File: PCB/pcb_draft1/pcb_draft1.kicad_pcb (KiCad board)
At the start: 2 copper layers, 100 x 100 mm, 53 parts, among them Q1 DMN6140L, Q10 DMN6140L, Q11 DMN6140L, Q12 DMN6140L, Q13 DMN6140L, Q14 DMN6140L, Q2 DMN6140L, Q3 DMN6140L, Q4 DMN6140L, Q5 DMN6140L, Q6 DMN6140L, Q7 DMN6140L, Q8 DMN6140L, Q9 DMN6140L, U1 STSPIN820, U2 STSPIN820

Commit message: add new netlist
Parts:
- added Arduino_FanControl1: Conn_01x01_Male, Connector_PinHeader_2.54mm:PinHeader_1x01_P2.54mm_Vertical, F.Cu at (177.5, -15.1)
- added D15: 1N4003, Diode_THT:D_DO-41_SOD81_P10.16mm_Horizontal, F.Cu at (165.0, -23.6)
- added Fan_Out1: Screw_Terminal_01x02, TerminalBlock_Phoenix:TerminalBlock_Phoenix_MKDS-1,5-2_1x02_P5.00mm_Horizontal, F.Cu at (166.6, -15.2)
- added Q15: DMN6140L, custom_symbols:SOT-223-edited, F.Cu at (182.0, -21.6)
- added R15: 200_Ohm_R, Resistor_SMD:R_0603_1608Metric, F.Cu at (189.4, -24.5)
- R1, R10, R11, R12, R13, R14, R2, R3, R4, R5, R6, R7, R8, R9: value R_Small -> 200_Ohm_R
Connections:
- U1 pad 2: GND -> 5V
- U1 pad 3: GND -> 5V
- U2 pad 2: GND -> 5V
- U2 pad 3: GND -> 5V

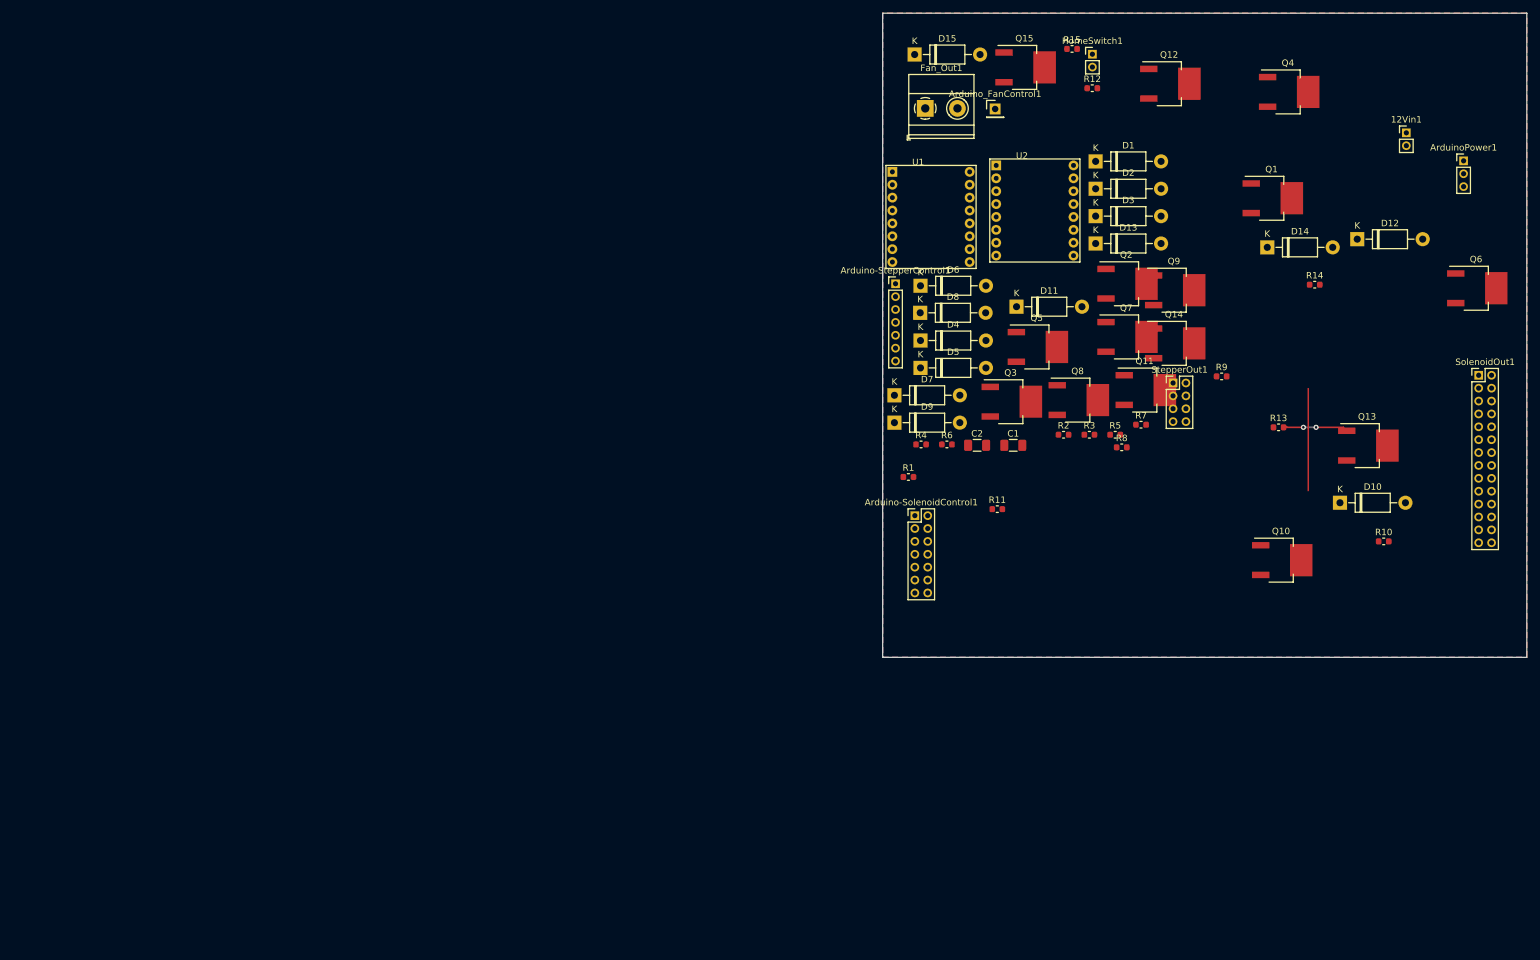
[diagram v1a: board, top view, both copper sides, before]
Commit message: Run traces for preliminarily finished board
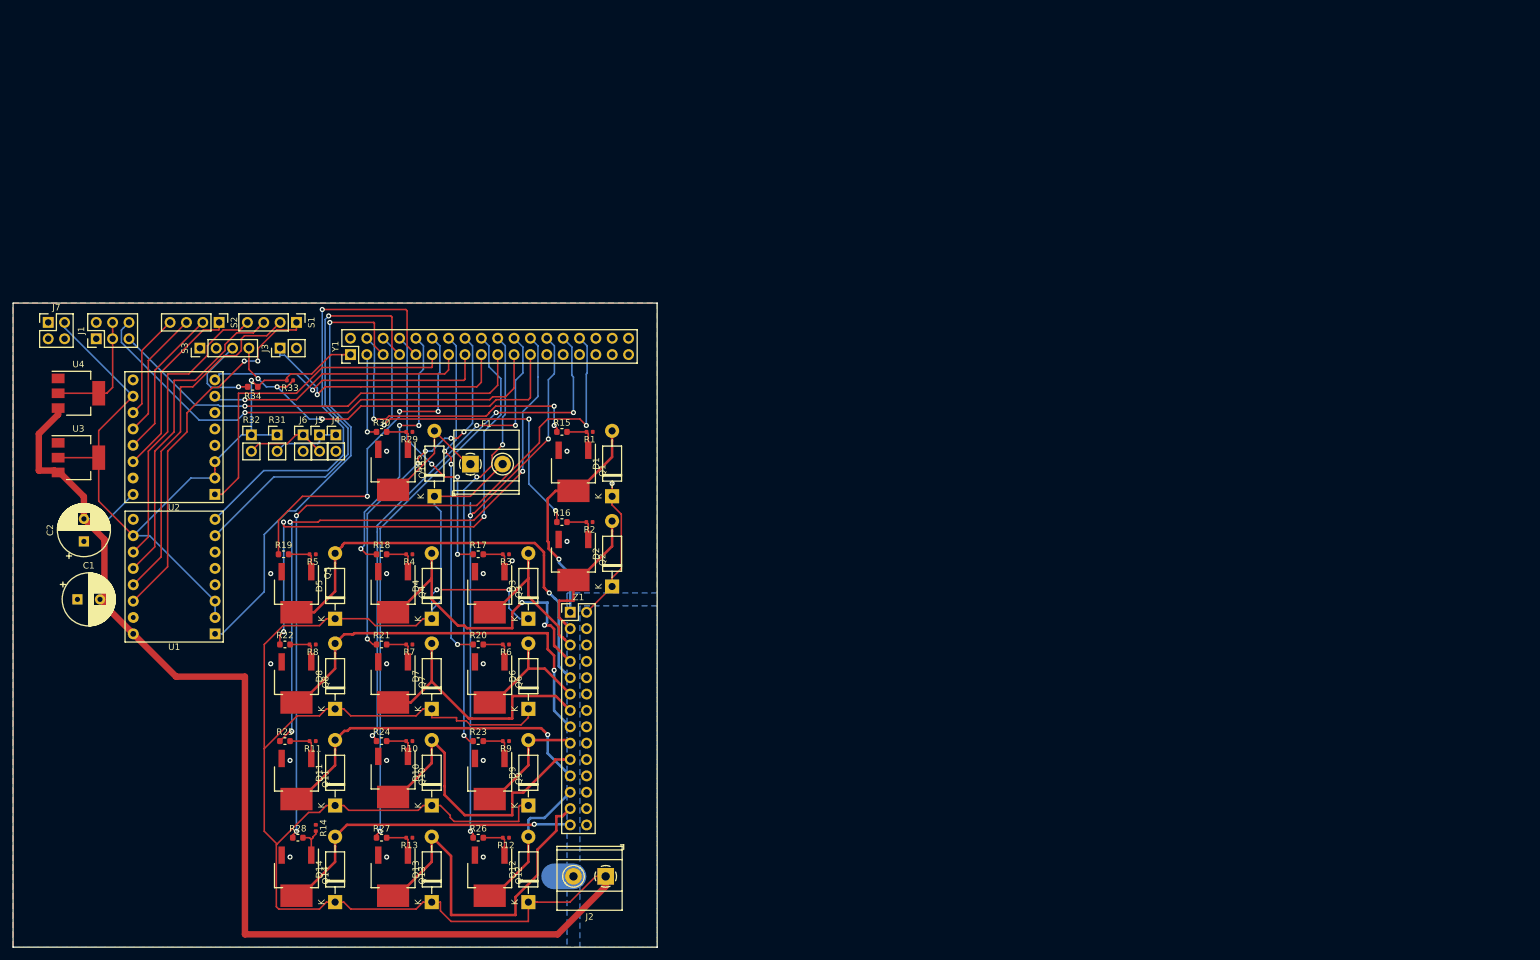
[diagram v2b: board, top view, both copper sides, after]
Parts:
- removed 12Vin1, HomeSwitch1: Conn_01x02_Male, Connector_PinHeader_2.00mm:PinHeader_1x02_P2.00mm_Vertical
- removed Arduino-SolenoidControl1: Conn_02x07_Odd_Even, Connector_PinHeader_2.00mm:PinHeader_2x07_P2.00mm_Vertical
- removed Arduino-StepperControl1: Conn_01x07_Male, Connector_PinHeader_2.00mm:PinHeader_1x07_P2.00mm_Vertical
- removed ArduinoPower1: Conn_01x03_Male, Connector_PinHeader_2.00mm:PinHeader_1x03_P2.00mm_Vertical
- removed Arduino_FanControl1: Conn_01x01_Male, Connector_PinHeader_2.54mm:PinHeader_1x01_P2.54mm_Vertical
- removed Fan_Out1: Screw_Terminal_01x02, TerminalBlock_Phoenix:TerminalBlock_Phoenix_MKDS-1,5-2_1x02_P5.00mm_Horizontal
- removed SolenoidOut1: Conn_02x14_Odd_Even, Connector_PinHeader_2.00mm:PinHeader_2x14_P2.00mm_Vertical
- removed StepperOut1: Conn_02x04_Odd_Even, Connector_PinHeader_2.00mm:PinHeader_2x04_P2.00mm_Vertical
- added F1: Fan_Screw_Terminal A97996-ND, TerminalBlock_Phoenix:TerminalBlock_Phoenix_MKDS-1,5-2_1x02_P5.00mm_Horizontal, F.Cu at (96.0, 40.0)
- added J1: RollerServos, Connector_PinHeader_2.54mm:PinHeader_2x03_P2.54mm_Vertical, F.Cu at (37.9, 20.5)
- added J2: 12V_Power A97996-ND, TerminalBlock_Phoenix:TerminalBlock_Phoenix_MKDS-1,5-2_1x02_P5.00mm_Horizontal, F.Cu at (117.0, 104.0)
- added J3: HomeSwitch, Connector_PinHeader_2.54mm:PinHeader_1x02_P2.54mm_Vertical, F.Cu at (66.5, 22.0)
- added J4: Therm1, Connector_PinHeader_2.54mm:PinHeader_1x02_P2.54mm_Vertical, F.Cu at (75.1, 35.5)
- added J5: ArdAnalogTherm, Connector_PinHeader_2.54mm:PinHeader_1x02_P2.54mm_Vertical, F.Cu at (72.6, 35.5)
- added J6: Therm2, Connector_PinHeader_2.54mm:PinHeader_1x02_P2.54mm_Vertical, F.Cu at (70.0, 35.5)
- added J7: Conn_02x02_Odd_Even, Connector_PinHeader_2.54mm:PinHeader_2x02_P2.54mm_Vertical, F.Cu at (30.5, 18.0)
- added R16: 200_Ohm_R, Resistor_SMD:R_0603_1608Metric, F.Cu at (110.2, 49.0)
- added R17: 200_Ohm_R, Resistor_SMD:R_0603_1608Metric, F.Cu at (97.2, 54.0)
- added R18: 200_Ohm_R, Resistor_SMD:R_0603_1608Metric, F.Cu at (82.2, 54.0)
- added R19: 200_Ohm_R, Resistor_SMD:R_0603_1608Metric, F.Cu at (67.0, 54.0)
- added R20: 200_Ohm_R, Resistor_SMD:R_0603_1608Metric, F.Cu at (97.2, 68.0)
- added R21: 200_Ohm_R, Resistor_SMD:R_0603_1608Metric, F.Cu at (82.2, 68.0)
- added R22: 200_Ohm_R, Resistor_SMD:R_0603_1608Metric, F.Cu at (67.2, 68.0)
- added R23: 200_Ohm_R, Resistor_SMD:R_0603_1608Metric, F.Cu at (97.2, 83.0)
- added R24: 200_Ohm_R, Resistor_SMD:R_0603_1608Metric, F.Cu at (82.2, 83.0)
- added R25: 200_Ohm_R, Resistor_SMD:R_0603_1608Metric, F.Cu at (67.2, 83.0)
- added R26: 200_Ohm_R, Resistor_SMD:R_0603_1608Metric, F.Cu at (97.2, 98.0)
- added R27: 200_Ohm_R, Resistor_SMD:R_0603_1608Metric, F.Cu at (82.2, 98.0)
- added R28: 200_Ohm_R, Resistor_SMD:R_0603_1608Metric, F.Cu at (69.2, 98.0)
- added R29: 10K_Ohm_R, Resistor_SMD:R_0402_1005Metric, F.Cu at (86.5, 35.0)
- added R30: 200_Ohm_R, Resistor_SMD:R_0603_1608Metric, F.Cu at (82.2, 35.0)
- added R31: ThermistorR, Connector_PinHeader_2.54mm:PinHeader_1x02_P2.54mm_Vertical, F.Cu at (66.0, 35.5)
- added R32: ThermistorR, Connector_PinHeader_2.54mm:PinHeader_1x02_P2.54mm_Vertical, F.Cu at (62.0, 35.5)
- added R33: 2.7k_Ohm_Res, Resistor_SMD:R_0402_1005Metric, F.Cu at (68.0, 27.0)
- added R34: 250_Ohm_Resistor, Resistor_SMD:R_0603_1608Metric, F.Cu at (62.2, 28.0)
- added S1: StepperMotor1, Connector_PinHeader_2.54mm:PinHeader_1x04_P2.54mm_Vertical, F.Cu at (69.0, 18.0)
- added S2: StepperMotor2, Connector_PinHeader_2.54mm:PinHeader_1x04_P2.54mm_Vertical, F.Cu at (57.0, 18.0)
- added S3: PaperHome, Connector_PinHeader_2.54mm:PinHeader_1x04_P2.54mm_Vertical, F.Cu at (54.0, 22.0)
- added U3: AMS1117-5.0 RasPi, Package_TO_SOT_SMD:SOT-223-3_TabPin2, F.Cu at (35.1, 39.0)
- added U4: AMS1117-5.0 Servo, Package_TO_SOT_SMD:SOT-223-3_TabPin2, F.Cu at (35.1, 29.0)
- added Y1: Arduino_Mega_Bottom_Pins1, Connector_PinHeader_2.54mm:PinHeader_2x18_P2.54mm_Vertical, F.Cu at (77.4, 23.0)
- added Z1: SolenoidOut, Connector_PinHeader_2.54mm:PinHeader_2x14_P2.54mm_Vertical, F.Cu at (111.5, 63.0)
- C1, C2: footprint Capacitor_SMD:C_1206_3216Metric -> Capacitor_THT:CP_Radial_D8.0mm_P3.50mm
- R1, R10, R11, R12, R13, R14, R2, R3, R4, R5, R6, R7, R8, R9: value 200_Ohm_R -> 10K_Ohm_R; footprint Resistor_SMD:R_0603_1608Metric -> Resistor_SMD:R_0402_1005Metric
- moved D14 176.8 mm to (75.0, 108.0), turned to 90 degrees
- moved R14 176.5 mm to (72.0, 96.5), turned to 270 degrees
- moved Q13 165.3 mm to (84.0, 103.8), turned to 270 degrees
- moved Q6 164.9 mm to (99.0, 73.8), turned to 270 degrees
- moved D12 164.8 mm to (105.0, 108.0), turned to 90 degrees
- moved Q12 162.0 mm to (99.0, 103.8), turned to 270 degrees
- moved Q14 159.3 mm to (69.0, 103.8), turned to 270 degrees
- moved Q4 159.1 mm to (84.0, 59.9), turned to 270 degrees
- moved R10 154.4 mm to (86.5, 83.0), turned to 180 degrees
- moved R13 149.2 mm to (86.5, 98.0), turned to 180 degrees
- moved D10 148.6 mm to (90.0, 93.0), turned to 90 degrees
- moved R12 147.7 mm to (101.5, 98.0), turned to 180 degrees
- moved C1 147.2 mm to (35.0, 61.0)
- moved D13 145.2 mm to (90.0, 108.0), turned to 90 degrees
- moved Q11 144.8 mm to (69.0, 88.8), turned to 270 degrees
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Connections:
- R1 pad 1: Net-(Arduino-SolenoidControl1-Pad5) -> GND
- R10 pad 1: Net-(Arduino-SolenoidControl1-Pad11) -> GND
- R11 pad 1: Net-(Arduino-SolenoidControl1-Pad6) -> GND
- R12 pad 1: Net-(Arduino-SolenoidControl1-Pad10) -> GND
- R13 pad 1: Net-(Arduino-SolenoidControl1-Pad14) -> GND
- R14 pad 1: Net-(Arduino-SolenoidControl1-Pad2) -> GND
- R15 pad 2: Net-(Q15-Pad1) -> Net-(Q1-Pad1)
- R2 pad 1: Net-(Arduino-SolenoidControl1-Pad1) -> GND
- R3 pad 1: Net-(Arduino-SolenoidControl1-Pad9) -> GND
- R4 pad 1: Net-(Arduino-SolenoidControl1-Pad8) -> GND
- R5 pad 1: Net-(Arduino-SolenoidControl1-Pad12) -> GND
- R6 pad 1: Net-(Arduino-SolenoidControl1-Pad13) -> GND
- R7 pad 1: Net-(Arduino-SolenoidControl1-Pad4) -> GND
- R8 pad 1: Net-(Arduino-SolenoidControl1-Pad7) -> GND
- R9 pad 1: Net-(Arduino-SolenoidControl1-Pad3) -> GND
- U1 pad 1: Net-(Arduino-StepperControl1-Pad1) -> StD1En
- U1 pad 7: Net-(Arduino-StepperControl1-Pad2) -> StD1St
- U1 pad 8: Net-(Arduino-StepperControl1-Pad3) -> StD1Dir
- U2 pad 1: Net-(Arduino-StepperControl1-Pad4) -> StD2En
- U2 pad 7: Net-(Arduino-StepperControl1-Pad5) -> StD2St
- U2 pad 8: Net-(Arduino-StepperControl1-Pad6) -> StD2Dir
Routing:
- net 12V: track 0.00 -> 476.8 mm, vias 0 -> 3
- net 5V: track 0.00 -> 124.6 mm, vias 0 -> 1
- net Net-(R28-Pad1): track 0.00 -> 117.3 mm, vias 0 -> 3
- net Net-(R27-Pad1): track 0.00 -> 98.6 mm, vias 0 -> 3
- net Net-(R25-Pad1): track 0.00 -> 96.6 mm, vias 0 -> 3
- net Net-(R26-Pad1): track 0.00 -> 85.7 mm, vias 0 -> 3
- net Net-(R22-Pad1): track 0.00 -> 81.7 mm, vias 0 -> 3
- net Servo2: track 0.00 -> 76.8 mm, vias 0 -> 1
- net Net-(R24-Pad1): track 0.00 -> 76.6 mm, vias 0 -> 3
- net StD1En: track 0.00 -> 72.2 mm, vias 0 -> 1
- net StD1Dir: track 0.00 -> 68.6 mm, vias 0 -> 1
- net Net-(D5-Pad2): track 0.00 -> 68.2 mm, vias 0 -> 1
- net Servo1: track 0.00 -> 67.7 mm, vias 0 -> 1
- net Net-(R23-Pad1): track 0.00 -> 66.9 mm, vias 0 -> 3
- net StD1St: track 0.00 -> 65.3 mm, vias 0 -> 1
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- added copper zone on B.Cu, net 12V

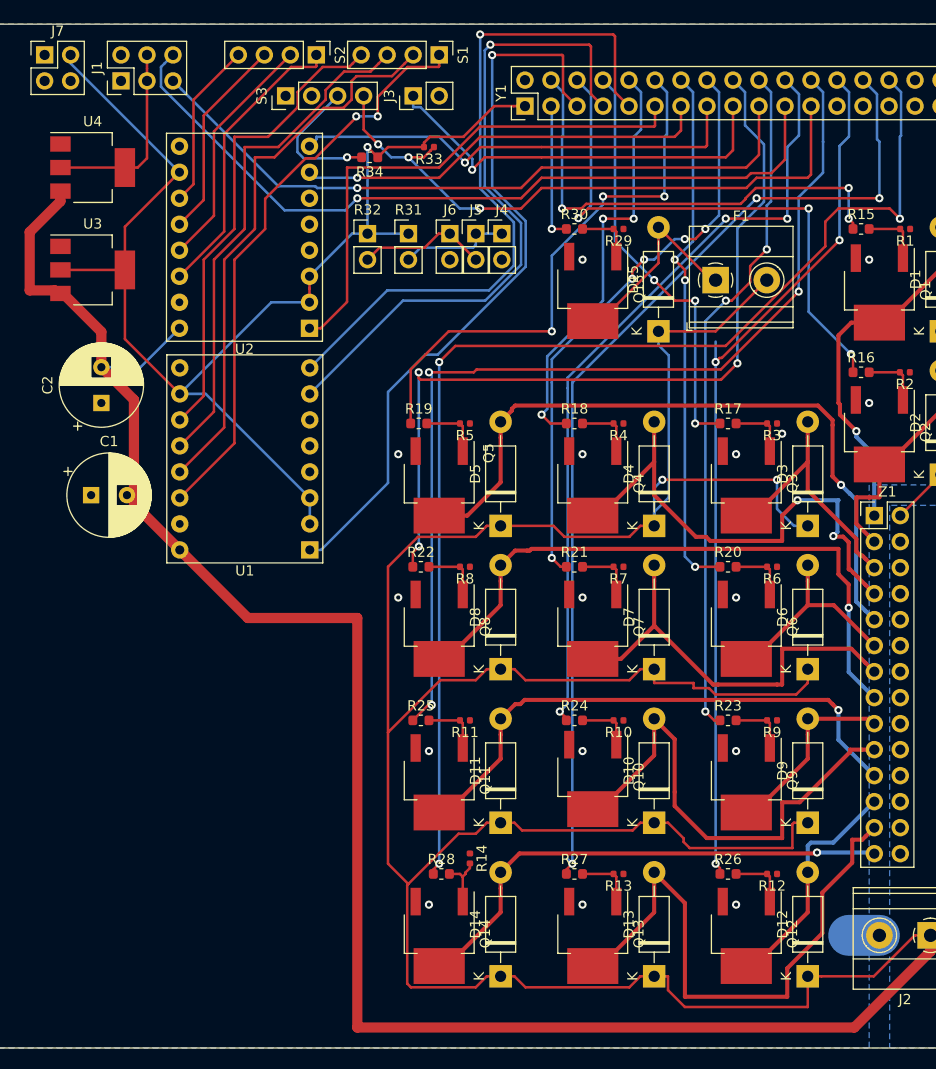
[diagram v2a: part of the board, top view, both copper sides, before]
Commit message: Run traces for preliminarily finished board
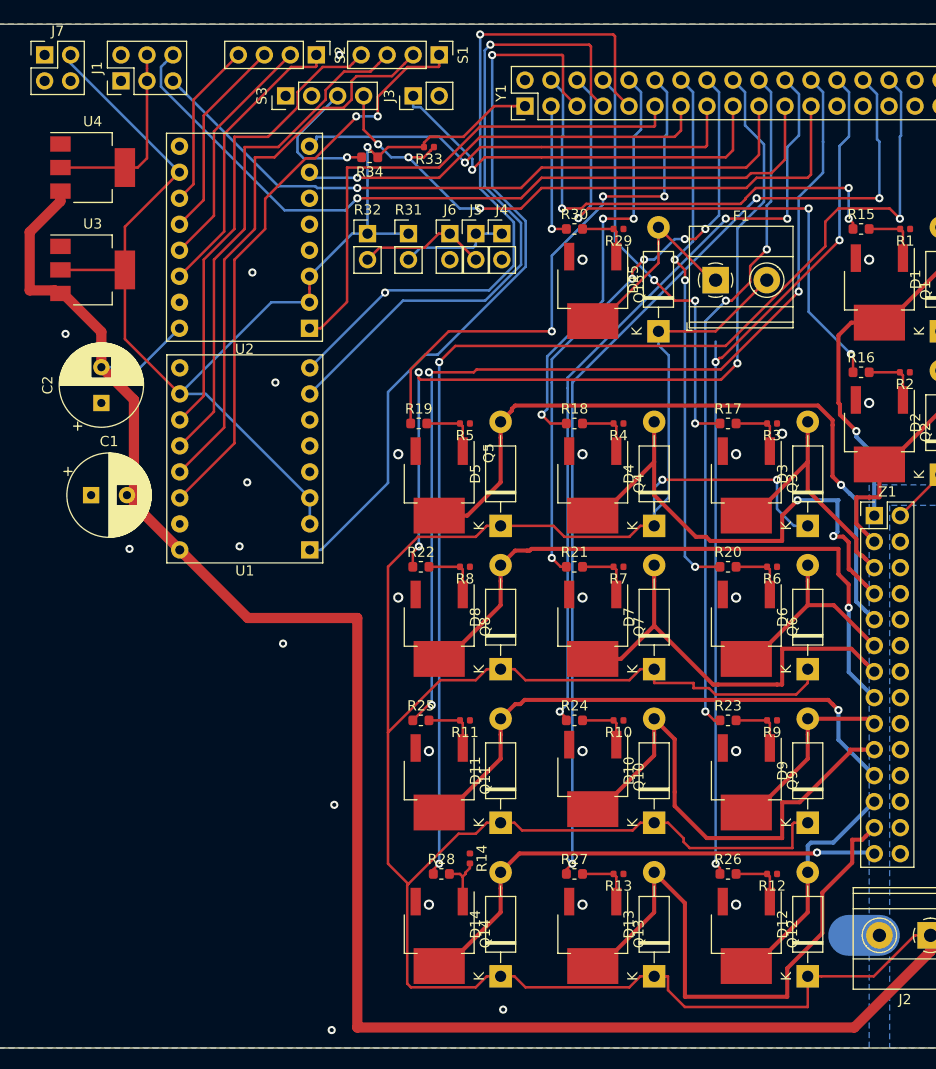
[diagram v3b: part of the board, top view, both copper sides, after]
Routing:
- net StD1Dir: vias 1 -> 2
- net GND: vias 16 -> 27
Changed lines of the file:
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@@
     (thickness 1.6)
     (drawings 4)
-    (tracks 824)
+    (tracks 837)
     (zones 0)
     (modules 83)
@@
     (0 F.Cu signal)
     (31 B.Cu signal)
-    (32 B.Adhes user)
-    (33 F.Adhes user)
-    (34 B.Paste user)
-    (35 F.Paste user)
-    (36 B.SilkS user)
-    (37 F.SilkS user)
-    (38 B.Mask user)
-    (39 F.Mask user)
+    (32 B.Adhes user hide)
+    (33 F.Adhes user hide)
+    (34 B.Paste user hide)
+    (35 F.Paste user hide)
+    (36 B.SilkS user hide)
+    (37 F.SilkS user hide)
+    (38 B.Mask user hide)
+    (39 F.Mask user hide)
     (40 Dwgs.User user)
     (41 Cmts.User user)
@@
   (segment (start 95.97499 80.47499) (end 103.87501 80.47499) (width 0.25) (layer F.Cu) (net 1))
   (segment (start 112 104) (end 109 104) (width 4) (layer B.Cu) (net 2))
-  (via (at 68 101) (size 0.8) (drill 0.4) (layers F.Cu B.Cu) (net 2))
-  (via (at 83 101) (size 0.8) (drill 0.4) (layers F.Cu B.Cu) (net 2))
-  (via (at 98 101) (size 0.8) (drill 0.4) (layers F.Cu B.Cu) (net 2))
-  (via (at 98 86) (size 0.8) (drill 0.4) (layers F.Cu B.Cu) (net 2))
-  (via (at 83 86) (size 0.8) (drill 0.4) (layers F.Cu B.Cu) (net 2))
-  (via (at 68 86) (size 0.8) (drill 0.4) (layers F.Cu B.Cu) (net 2))
-  (via (at 65 57) (size 0.8) (drill 0.4) (layers F.Cu B.Cu) (net 2))
-  (via (at 83 57) (size 0.8) (drill 0.4) (layers F.Cu B.Cu) (net 2))
-  (via (at 98 57) (size 0.8) (drill 0.4) (layers F.Cu B.Cu) (net 2))
-  (via (at 111 52) (size 0.8) (drill 0.4) (layers F.Cu B.Cu) (net 2))
-  (via (at 111 38) (size 0.8) (drill 0.4) (layers F.Cu B.Cu) (net 2))
-  (via (at 83 38) (size 0.8) (drill 0.4) (layers F.Cu B.Cu) (net 2))
-  (via (at 83 71) (size 0.8) (drill 0.4) (layers F.Cu B.Cu) (net 2))
-  (via (at 65 71) (size 0.8) (drill 0.4) (layers F.Cu B.Cu) (net 2))
-  (via (at 98 71) (size 0.8) (drill 0.4) (layers F.Cu B.Cu) (net 2))
-  (via (at 102.5 55) (size 0.8) (drill 0.4) (layers F.Cu B.Cu) (net 2))
+  (via (at 68 101) (size 1) (drill 0.6) (layers F.Cu B.Cu) (net 2))
+  (via (at 83 101) (size 1) (drill 0.6) (layers F.Cu B.Cu) (net 2))
+  (via (at 98 101) (size 1) (drill 0.6) (layers F.Cu B.Cu) (net 2))
+  (via (at 98 86) (size 1) (drill 0.6) (layers F.Cu B.Cu) (net 2))
+  (via (at 83 86) (size 1) (drill 0.6) (layers F.Cu B.Cu) (net 2))
+  (via (at 68 86) (size 1) (drill 0.6) (layers F.Cu B.Cu) (net 2))
+  (via (at 65 57) (size 1) (drill 0.6) (layers F.Cu B.Cu) (net 2))
+  (via (at 83 57) (size 1) (drill 0.6) (layers F.Cu B.Cu) (net 2))
+  (via (at 98 57) (size 1) (drill 0.6) (layers F.Cu B.Cu) (net 2))
+  (via (at 111 52) (size 1) (drill 0.6) (layers F.Cu B.Cu) (net 2))
+  (via (at 111 38) (size 1) (drill 0.6) (layers F.Cu B.Cu) (net 2))
+  (via (at 83 38) (size 1) (drill 0.6) (layers F.Cu B.Cu) (net 2))
+  (via (at 83 71) (size 1) (drill 0.6) (layers F.Cu B.Cu) (net 2))
+  (via (at 65 71) (size 1) (drill 0.6) (layers F.Cu B.Cu) (net 2))
+  (via (at 98 71) (size 1) (drill 0.6) (layers F.Cu B.Cu) (net 2))
+  (via (at 102.5 55) (size 1) (drill 0.6) (layers F.Cu B.Cu) (net 2))
+  (via (at 32.5 45.25) (size 0.8) (drill 0.4) (layers F.Cu B.Cu) (net 2))
+  (via (at 38.75 66.25) (size 0.8) (drill 0.4) (layers F.Cu B.Cu) (net 2))
+  (via (at 53.75 75.5) (size 0.8) (drill 0.4) (layers F.Cu B.Cu) (net 2))
+  (via (at 58.75 91.25) (size 0.8) (drill 0.4) (layers F.Cu B.Cu) (net 2))
+  (via (at 58.5 113.25) (size 0.8) (drill 0.4) (layers F.Cu B.Cu) (net 2))
+  (via (at 75.25 111.25) (size 0.8) (drill 0.4) (layers F.Cu B.Cu) (net 2))
+  (via (at 49.5 66) (size 0.8) (drill 0.4) (layers F.Cu B.Cu) (net 2))
+  (via (at 50.25 59.75) (size 0.8) (drill 0.4) (layers F.Cu B.Cu) (net 2))
+  (via (at 53 50) (size 0.8) (drill 0.4) (layers F.Cu B.Cu) (net 2))
+  (via (at 50.75 39.25) (size 0.8) (drill 0.4) (layers F.Cu B.Cu) (net 2))
+  (via (at 59.25 18) (size 0.8) (drill 0.4) (layers F.Cu B.Cu) (net 2))
   (segment (start 64 27) (end 63 28) (width 0.25) (layer F.Cu) (net 3))
   (segment (start 67.515 27) (end 64 27) (width 0.25) (layer F.Cu) (net 3))
@@
   (segment (start 73 31.054998) (end 76.295001 34.349999) (width 0.25) (layer B.Cu) (net 54))
   (segment (start 73.859002 41) (end 63.93 41) (width 0.25) (layer B.Cu) (net 54))
-  (segment (start 63.93 41) (end 56.36 48.57) (width 0.25) (layer B.Cu) (net 54))
+  (segment (start 63.93 41) (end 63.715 41.215) (width 0.25) (layer B.Cu) (net 54))
+  (segment (start 63.715 41.215) (end 56.36 48.57) (width 0.25) (layer B.Cu) (net 54))
+  (via (at 63.715 41.215) (size 0.8) (drill 0.4) (layers F.Cu B.Cu) (net 54))
   (segment (start 83.824999 21.824999) (end 83.824999 17.175001) (width 0.25) (layer F.Cu) (net 55))
   (segment (start 85 23) (end 83.824999 21.824999) (width 0.25) (layer F.Cu) (net 55))
